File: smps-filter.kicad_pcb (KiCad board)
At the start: 2 copper layers, 13 parts, among them J1 Power IN, J2 Power OUT 1, J3 Power OUT 2, J4 Power OUT 3

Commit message: Finalied schema and PCB
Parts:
- added H1: MountingHole_Pad, MountingHole:MountingHole_2.2mm_M2_DIN965_Pad_TopBottom, F.Cu at (102.8, 51.5)
- added H2: MountingHole_Pad, MountingHole:MountingHole_2.2mm_M2_DIN965_Pad_TopBottom, F.Cu at (132.2, 51.5)
- added H3: MountingHole_Pad, MountingHole:MountingHole_2.2mm_M2_DIN965_Pad_TopBottom, F.Cu at (102.8, 98.5)
- added H4: MountingHole_Pad, MountingHole:MountingHole_2.2mm_M2_DIN965_Pad_TopBottom, B.Cu at (132.2, 98.5)
- D1: footprint Diode_SMD:D_SMP_DO-220AA -> smps-filter:DO214AA
- J1, J2: footprint TerminalBlock_MetzConnect:TerminalBlock_MetzConnect_Type171_RT13702HBWC_1x02_P7.50mm_Horizontal -> smps-filter:TerminalBlock_1x02_P7.50mm_Horizontal
- L1, L2: footprint Inductor_SMD:L_10.4x10.4_H4.8 -> smps-filter:L_10.4x10.4_H4.8
- moved J3 5.96 mm to (124.8, 90.5), turned to 0 degrees
- moved J1 4.92 mm to (117.5, 59.5)
- moved J2 4.24 mm to (117.0, 90.5)
- moved J4 4.24 mm to (124.8, 97.5), turned to 0 degrees
- moved D1 0.85 mm to (106.0, 60.5)
- turned C2 to -90 degrees
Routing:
- net Vout: track 18.7 -> 78.9 mm
- net Vin: track 7.28 -> 38.2 mm
- net GND: track 0.00 -> 0.28 mm, vias 8 -> 10
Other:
- board outline added: 35 x 52.5 mm
- board text added: "${COMMENT8} ${COMMENT9} ${REVISION} ${ISSUE_DATE}"
- board text added: "+ OUTPUT -"
- board text added: "- INPUT +"
- board text added: "- OUTPUT +"
- board text added: "GND"
- board text added: "VIN"
- board text added: "VOUT"

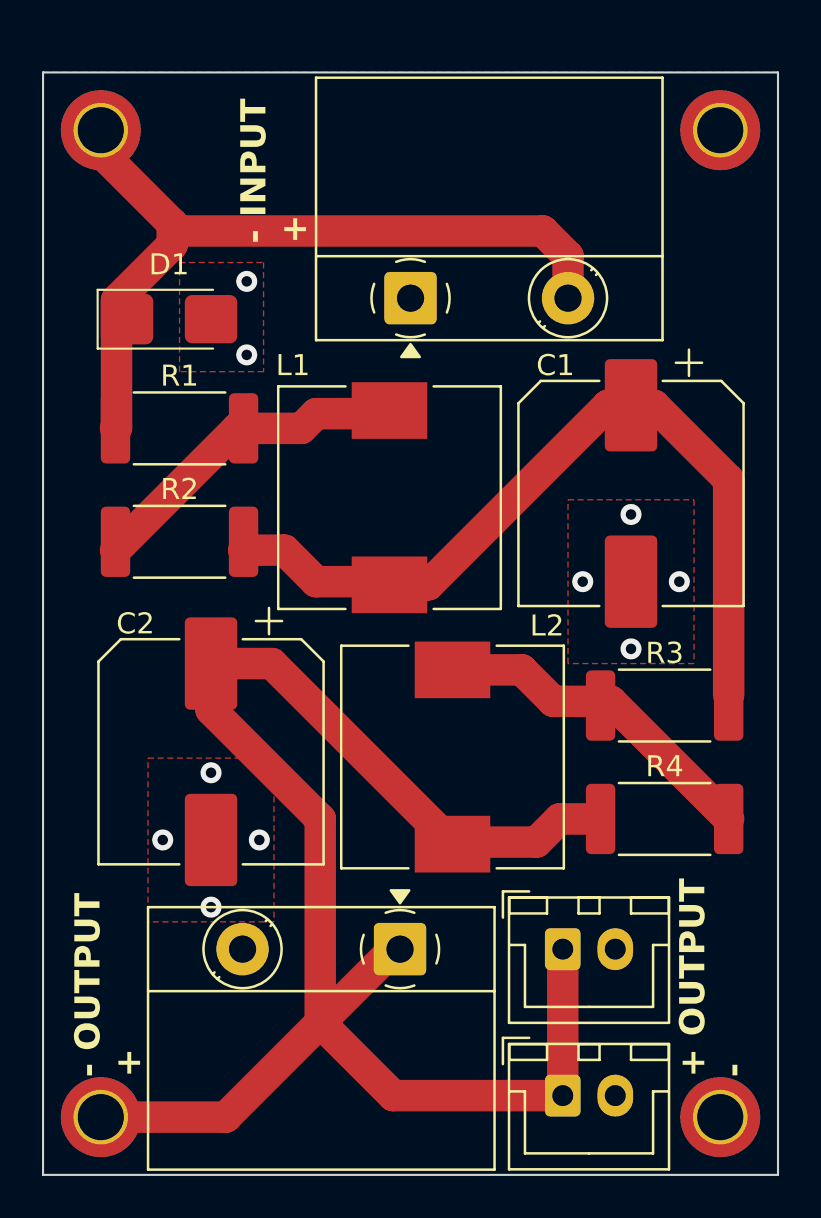
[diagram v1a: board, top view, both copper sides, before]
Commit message: Implement GitHub workflows for release and testing
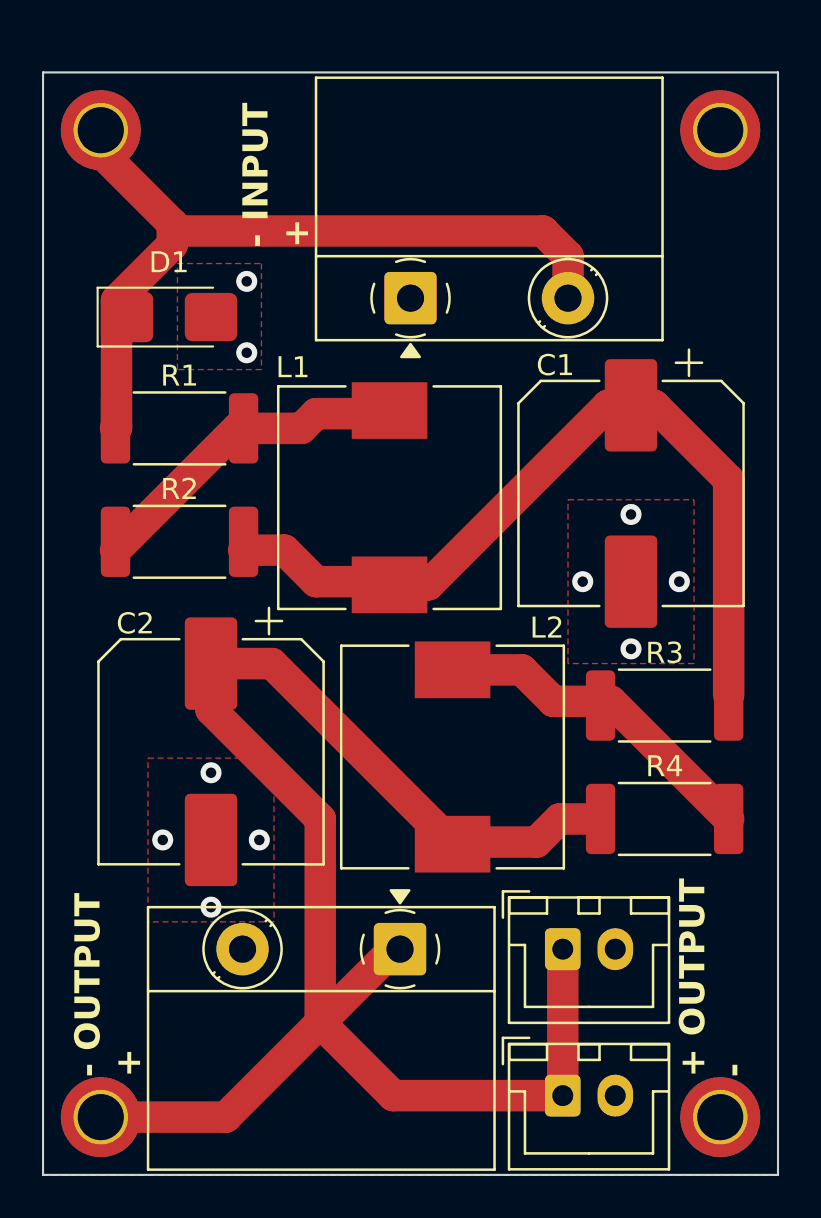
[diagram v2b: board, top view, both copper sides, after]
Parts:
- moved D1 0.10 mm to (106.0, 60.4)
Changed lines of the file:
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@@
 		(tags "Choke SMD")
 		(property "Reference" "L2"
-			(at -6.25 -4.5 180)
+			(at -6.15 -4.5 180)
 			(layer "F.SilkS")
 			(effects
@@
 		(tags "Choke SMD")
 		(property "Reference" "L1"
-			(at -6.3 4.6 180)
+			(at -6.2 4.6 180)
 			(layer "F.SilkS")
 			(effects
@@
 	(footprint "smps-filter:DO214AA"
 		(layer "F.Cu")
-		(at 106 60.5)
+		(at 106 60.4)
 		(property "Reference" "D1"
 			(at 0 -2.6 0)
@@
 	)
 	(gr_text "- INPUT\n+"
-		(at 111 56.9 90)
+		(at 111.1 57.1 90)
 		(layer "F.SilkS" knockout)
 		(effects
@@
 	)
 	(gr_text "${COMMENT8}\n${COMMENT9}\n${REVISION} ${ISSUE_DATE}\n"
-		(at 105.9 53.5 90)
+		(at 130.2 55 0)
 		(layer "B.SilkS" knockout)
 		(effects
@@
 	)
 	(gr_text "VIN"
-		(at 105.8 51.6 0)
+		(at 102.7 54.2 0)
 		(layer "B.SilkS")
 		(effects
@@
 	)
 	(gr_text "GND"
-		(at 128.8 51.5 0)
+		(at 132.2 54.2 0)
 		(layer "B.SilkS")
 		(effects
@@
 	)
 	(gr_text "VOUT"
-		(at 106.7 98.5 0)
+		(at 102.7 95.8 0)
 		(layer "B.SilkS")
 		(effects
@@
 	)
 	(via
-		(at 109.7 62.2)
+		(at 109.7 62.1)
 		(size 1)
 		(drill 0.5)
@@
 		(polygon
 			(pts
-				(xy 106.5 57.8) (xy 110.5 57.8) (xy 110.5 63) (xy 106.5 63)
+				(xy 106.4 57.85) (xy 110.4 57.85) (xy 110.4 62.9) (xy 106.4 62.9)
 			)
 		)
